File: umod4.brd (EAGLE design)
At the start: 104.9 x 69.8 mm, 94 parts, among them IC3 27C256-FEED-THRU, J2 10118194-0001LF, M1 RPi Pico W, M2 Generic single-sided NEO-8, Q1 C10487/SI2301CDS, Q2 SS8050, Q3 C10487/SI2301CDS, Q4 C10487/SI2301CDS, U1 74LVC541, U2 74LVC4245, U3 74LVC541, U4 RP2040, U5 W25Q128JVSIQ, U6 74LVC2G04, U8 3.3V/150mA, Y1 12MHz

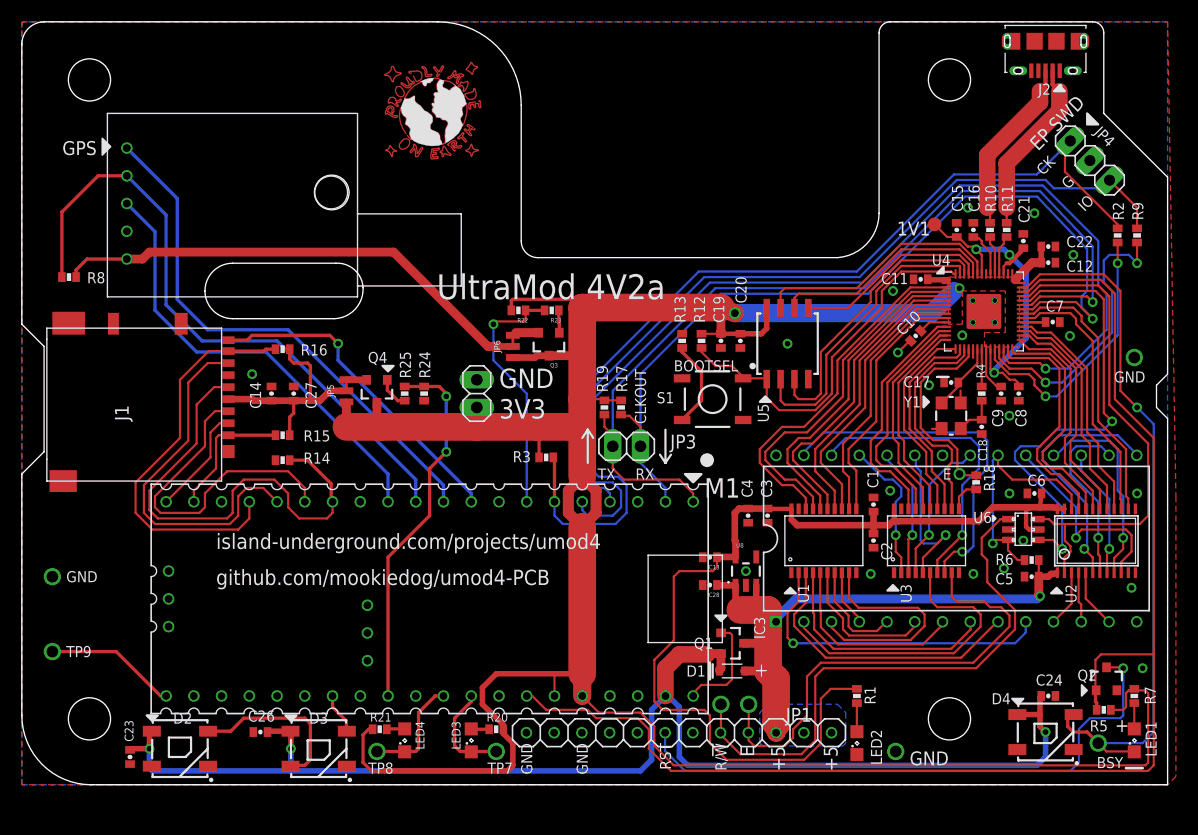
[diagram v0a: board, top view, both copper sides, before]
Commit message: 4v2a Release: add caps, DNP convention, production automation
Board changes:
- See Changelist-4V2.md for details

Tooling:
- Add preproduction.py: BOM generation (HTML + CSV), CPL generation via Eagle ULP batch mode, gerber freshness check, and ZIP packaging
- Add jlcpcb_smta_exporter_v7.ulp: modified to accept batch-mode arguments, bypassing interactive dialogs when invoked from script
- Update jlcpcb_2_layer_v72.cam: output path changed to build/cam/
- Update .gitignore: build/ directory rules with build/cam/.gitkeep anchor

Documentation:
- Add Production.md: describes end-to-end JLCPCB submission workflow
- Remove TestPlan.md
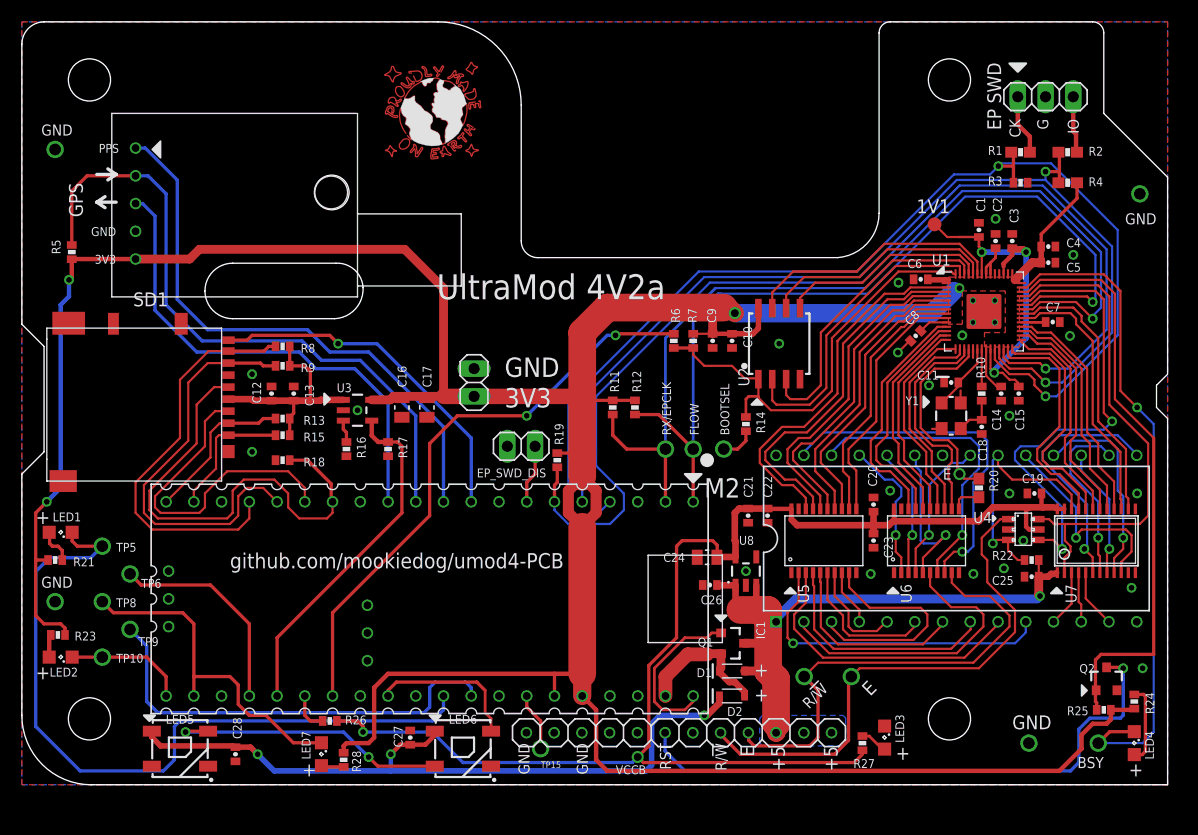
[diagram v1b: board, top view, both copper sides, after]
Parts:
- removed D3, D4: C2761795/WS2812B, SparkFun-LED:WS2812B
- removed J2: 10118194-0001LF, 10118194-0001LF:AMPHENOL_10118194-0001LF
- removed JP5, JP6: JUMPER-SMT_3_1-NC_TRACE_NO-SILK, SparkFun-Jumpers:SMT-JUMPER_3_1-NC_TRACE_NO-SILK
- removed Q3, Q4: C10487/SI2301CDS, robins-v7:SOT23
- removed S1: (no value), robins-v7:SW-TAC-5.2MM
- added C25: 100n/16V/X7R, SparkFun-03-01-2010:0402-CAP
- added LED5, LED6: WS2812, SparkFun-LED:WS2812B
- added LED7: NCD0805R1, led:SML0805
- added R26: 10K, SparkFun-03-01-2010:0402-RES
- added R27: 1K, SparkFun-03-01-2010:0402-RES
- added R28: 470R, SparkFun-03-01-2010:0402-RES
- added TP10, TP11, TP12, TP13, TP14, TP15, TP16: 1035, robins-v7:KEYSTONE-1035
- added U7: 74LVC4245, robins-v7:TSSOP-24
- C10, C3: value 100n/16V/X7R -> 2u2/6.3V/X5R
- C11: value 100n/16V/X7R -> 33p/6.3V/COG
- C13: value 1u/25V/X5R -> 4u7/10V/X5R
- C16, C24: value 100n/16V/X7R -> 10u/25V/X5R; device SparkFun-03-01-2010:0402-CAP -> robins-v7:SMD-0805
- C17: value 33p/6.3V/COG -> 10u/25V/X5R; device SparkFun-03-01-2010:0402-CAP -> robins-v7:SMD-0805
- C2, C28: value 1u/25V/X5R -> 100n/16V/X7R
- C20, C22: value 2u2/6.3V/X5R -> 100n/16V/X7R
- C21: value 2u2/6.3V/X5R -> 1u/25V/X5R
- C23: value 100n/16V/X7R -> 1u/25V/X5R
- C26: value 100n/16V/X7R -> 4u7/10V/X5R
- C27: value 4u7/10V/X5R -> 100n/16V/X7R
- C4: value 1u/25V/X5R -> 2u2/6.3V/X5R
- D2: value C2761795/WS2812B -> 1N5819WS; device SparkFun-LED:WS2812B -> SparkFun-DiscreteSemi:SOD-323
- JP1: value PINHD-1X12 -> (none); device robins:1X12 -> pinhead:1X03
- JP4: value (none) -> PINHD-1X12; device pinhead:1X03 -> robins:1X12
- LED3: value KT-0805G -> KT-0805Y
- M1: value RPi Pico W -> Generic single-sided NEO-8; device robins-v7:PICO-TH -> robins-v7:GPS-MODULE-DS
- M2: value Generic single-sided NEO-8 -> RPi Pico W; device robins-v7:GPS-MODULE-DS -> robins-v7:PICO-TH
- Q1: value C10487/SI2301CDS -> DNP/SI2301CDS
- R1: value 1K -> 100R; device SparkFun-03-01-2010:0402-RES -> SparkFun-03-01-2010:0603-RES
- R10: value 27R -> 1K
- R11, R18: value 27R -> 10K
- R13, R25: value 1K -> 10K
- R14, R6: value 10K -> 1K
- R2: device SparkFun-03-01-2010:0402-RES -> SparkFun-03-01-2010:0603-RES
- R20: value 470R -> 100R; device SparkFun-03-01-2010:0402-RES -> SparkFun-03-01-2010:0603-RES
- R23: value 1K -> 470R
- R24: value 10K -> 470R
- R4: value 1K -> 4K7; device SparkFun-03-01-2010:0402-RES -> SparkFun-03-01-2010:0603-RES
- R7: value 470R -> 10K
- R9: value 100R -> 10K
- SD1: value (none) -> DM3AT-SF-PEJM5
- TP1, TP2, TP3, TP4, TP5, TP6, TP7, TP8, TP9: value (none) -> 1035
- U1: value 74LVC541 -> RP2040; device robins-v7:TSSOP-20 -> robins-v7:RP2040-QFN56
- U2: value 74LVC4245 -> W25Q128JVSIQ; device robins-v7:TSSOP-24 -> SparkFun-IC-Memory:SOIC-8
- U3: value 74LVC541 -> SY6280AAC; device robins-v7:TSSOP-20 -> robins-v7:SOT23-5
- U4: value RP2040 -> 74LVC2G04; device robins-v7:RP2040-QFN56 -> robins-v7:SOT23-6
- U5: value W25Q128JVSIQ -> 74LVC541; device SparkFun-IC-Memory:SOIC-8 -> robins-v7:TSSOP-20
- U6: value 74LVC2G04 -> 74LVC541; device robins-v7:SOT23-6 -> robins-v7:TSSOP-20
- U8: value 3.3V/150mA -> TLV75733P
- moved R5 103.4 mm to (4.57, 48.8), turned to 270 degrees
- moved LED1 100.1 mm to (3.56, 23.1), turned to 180 degrees
- moved R9 79.1 mm to (23.9, 38.4), turned to 0 degrees
- moved LED2 73.3 mm to (3.56, 11.7), turned to 180 degrees
- moved C12 72.1 mm to (22.9, 35.8), turned to 90 degrees
- moved C23 70.9 mm to (78.0, 22.4)
- moved R24 70.9 mm to (101.9, 7.62)
- moved R25 70.3 mm to (99.1, 6.86), turned to 0 degrees
- moved JP1 67.2 mm to (93.7, 63.0)
- moved LED4 66.8 mm to (101.9, 3.81), turned to 270 degrees
- moved C14 66.8 mm to (89.7, 35.8), turned to 270 degrees
- moved JP4 64.5 mm to (60.2, 4.76), turned to 0 degrees
- moved R18 63.5 mm to (23.9, 29.7), turned to 180 degrees
- moved TP4 62.6 mm to (64.3, 30.7)
- moved TP5 60.9 mm to (7.37, 21.8)
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- renumbered IC3 to IC1, J1 to SD1
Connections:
- removed net 3V3_GPS_EN: M1.7, R22.1, R23.2
- removed net 3V3_SD_EN: M1.29, R24.2, R25.1
- removed net 3V3_SD_SW: JP5.3, Q4.S
- removed net 3V3_SW: JP6.3, Q3.S
- removed net N$15: R10.2, U4.47
- removed net N$16: R9.1, U4.25
- removed net N$17: J2.2, R11.1
- removed net N$18: J2.3, R10.1
- removed net N$23: Q4.G, R25.2
- removed net N$25: Q3.G, R23.1
- removed net SPARE0: LED3.C, M1.32, TP7.P$1
- removed net SPARE1: LED4.C, M1.31, TP8.P$1
- removed net SPARE2: M1.21, TP9.P$1
- removed net VCC_GPS: JP6.2, M2.5, R8.2
- new net DISK_BSY: LED1.C, M2.31, TP5.P$1
- new net EN_VDD_SD: M2.25, R17.1, U3.4
- new net EP_BOOTSEL: M2.27, R6.2
- new net EP_SWD_DIS: JP3.1, M2.7
- new net EXT_RP_SWCLK: JP1.1, R1.2
- new net EXT_RP_SWD: JP1.3, R2.2
- new net SPARE0_ADC: M2.32, TP9.P$1
- new net SPARE3: LED2.C, M2.21, TP10.P$1
- new net SPARE4: LED7.C, M2.22, TP8.P$1
- new net SPARE5: M2.24, TP6.P$1
- new net SPARE6_ADC: M2.34, TP15.P$1
- new net VCCB_PWR: M2.26, R26.2
- new net VLED: C27.1, C28.1, D2.C, LED5.1, LED6.1
- net !CARD: now also M2.9; no longer M1.9
- net !CE!_5V: now also R22.1, U4.3, U7.22; no longer R6.1, U2.22, U6.3
- net !RESET!_5V: now also JP4.6; no longer JP1.6
- net !RESET!_HC11_OUT: now also R25.1, U1.40; no longer M1.34, R5.1, U4.40
- net +3V3: now also C14.1, C17.1, C2.1, C4.1, C5.1, C6.1, C8.1, M1.5, M2.35, M2.36, R11.1, R12.1, R19.2, R23.1, R24.1, R25.2, R28.1, R4.1, R7.2, U1.1, U1.10, U1.22, U1.33, U1.42, U1.43, U1.44, U1.48, U1.49, U2.8, U3.5; no longer C11.1, C12.1, C19.1, C20.1, C22.1, JP5.1, JP6.1, M1.35, M1.36, Q3.D, Q4.D, R12.2, R17.1, R19.1, R20.1, R22.2, R3.2, R7.1, U4.1, U4.10, U4.22, U4.33, U4.42, U4.43, U4.44, U4.48, U4.49, U5.8
- net +5_ECU: now also C25.1, C26.1, JP4.10, JP4.12, R22.2, U7.1; no longer C28.1, C5.1, JP1.10, JP1.12, R6.2, U2.1
- net 1.0V: now also C1.1, C3.1, U1.23, U1.45, U1.50; no longer C21.1, C8.1, U4.23, U4.45, U4.50
- net A0_5V: now also U5.2; no longer U1.2
- net A10_5V: now also U6.4; no longer U3.4
- net A11_5V: now also U6.5; no longer U3.5
- net A12_5V: now also U6.6; no longer U3.6
- net A13_5V: now also U6.7; no longer U3.7
- net A14_5V: now also U6.8; no longer U3.8
- net A1_5V: now also U5.3; no longer U1.3
- net A2_5V: now also U5.4; no longer U1.4
- net A3_5V: now also U5.5; no longer U1.5
- net A4_5V: now also U5.6; no longer U1.6
- net A5_5V: now also U5.7; no longer U1.7
- net A6_5V: now also U5.8; no longer U1.8
- net A7_5V: now also U5.9; no longer U1.9
- net A8_5V: now also U6.2; no longer U3.2
- net A9_5V: now also U6.3; no longer U3.3
- net CE: now also U1.38, U4.4; no longer U4.38, U6.4
- net D0: now also U1.27, U7.21; no longer U2.21, U4.27
- net D0_5V: now also U7.3; no longer U2.3
- net D1: now also U1.28, U7.20; no longer U2.20, U4.28
- net D1_5V: now also U7.4; no longer U2.4
- net D2: now also U1.29, U7.19; no longer U2.19, U4.29
- net D2_5V: now also U7.5; no longer U2.5
- net D3: now also U1.30, U7.18; no longer U2.18, U4.30
- net D3_5V: now also U7.6; no longer U2.6
- net D4: now also U1.31, U7.17; no longer U2.17, U4.31
- net D4_5V: now also U7.7; no longer U2.7
- net D5: now also U1.32, U7.16; no longer U2.16, U4.32
- net D5_5V: now also U7.8; no longer U2.8
- net D6: now also U1.34, U7.15; no longer U2.15, U4.34
- net D6_5V: now also U7.9; no longer U2.9
- net D7: now also U1.35, U7.14; no longer U2.14, U4.35
- net D7_5V: now also U7.10; no longer U2.10
- net DAT1: now also M2.17, R8.1; no longer M1.17, R16.1
- net DAT2: now also M2.19; no longer M1.19
- net DBG_BSY: now also LED4.C, TP14.P$1, U1.41; no longer D4.4, LED1.C, TP1.P$1, U4.41
- net E: now also R20.1, U1.18; no longer R18.1, U4.18
- net EP_RUN: now also M2.6, R19.1, U1.26; no longer M1.6, R3.1, U4.26
- net E_5V: now also JP4.9, TP11.P$1, U6.9; no longer JP1.9, TP5.P$1, U3.9
- net GND: now also C11.1, C17.2, C25.2, JP1.2, JP3.2, JP4.1, JP4.3, LED3.C, LED5.3, LED6.3, M1.4, M2.13, M2.18, M2.23, M2.28, M2.3, M2.33, M2.38, M2.42, M2.45, M2.8, R16.2, R17.2, R18.2, R3.2, TP1.P$1, TP13.P$1, TP16.P$1, TP7.P$1, U1.57, U1.GND@1, U1.GND@2, U1.GND@3, U1.GND@4, U2.4, U3.2, U4.2, U5.1, U5.10, U5.19, U6.1, U6.10, U6.19, U7.11, U7.12, U7.13; no longer C11.2, C17.1, D2.3, D3.3, D4.3, J2.5, JP1.1, JP1.3, JP4.2, LED2.C, M1.13, M1.18, M1.23, M1.28, M1.3, M1.33, M1.38, M1.42, M1.45, M1.8, M2.4, R13.2, R14.2, R24.1, TP2.P$1, TP3.P$1, TP4.P$1, U1.1, U1.10, U2.11, U2.12, U2.13, U3.1, U3.10, U3.19, U4.19, U4.57, U4.GND@1, U4.GND@2, U4.GND@3, U4.GND@4, U5.4, U6.2
- net GPS_PPS: now also M1.1, M2.10; no longer M1.10, M2.1
- net IO0: now also U1.2, U5.18; no longer U1.18, U4.2
- net IO1: now also U1.3, U5.17; no longer U1.17, U4.3
- net IO10: now also U1.13, U6.16; no longer U3.16, U4.13
- net IO11: now also U1.14, U6.15; no longer U3.15, U4.14
- net IO12: now also U1.15, U6.14; no longer U3.14, U4.15
- net IO13: now also U1.16, U6.13; no longer U3.13, U4.16
- net IO14: now also U1.17, U6.12; no longer U3.12, U4.17
- net IO2: now also U1.4, U5.16; no longer U1.16, U4.4
- net IO3: now also U1.5, U5.15; no longer U1.15, U4.5
- net IO4: now also U1.6, U5.14; no longer U1.14, U4.6
- net IO5: now also U1.7, U5.13; no longer U1.13, U4.7
- net IO6: now also U1.8, U5.12; no longer U1.12, U4.8
- net IO7: now also U1.9, U5.11; no longer U1.11, U4.9
- net IO8: now also U1.11, U6.18; no longer U3.18, U4.11
- net IO9: now also U1.12, U6.17; no longer U3.17, U4.12
- net N$1: now also R10.2; no longer R4.2
- net N$10: now also U1.55, U2.2; no longer U4.55, U5.2
- net N$11: now also U1.54, U2.3; no longer U4.54, U5.3
- net N$12: now also U1.51, U2.7; no longer U4.51, U5.7
- net N$13: now also LED2.A, R23.2; no longer R11.2, U4.46
- net N$14: now also R16.1, U3.3; no longer R13.1, S1.1@1, S1.1@2
- net N$19: now also LED5.4, LED6.2; no longer D2.4, D3.2
- net N$2: now also C11.2, U1.20; no longer C17.2, U4.20
- net N$20: now also R20.2, U6.11; no longer R18.2, U3.11
- net N$21: now also LED1.A, R21.2; no longer LED3.A, R20.2
- net N$22: now also LED7.A, R28.2; no longer LED4.A, R21.2
- net N$3: now also LED3.A, R27.2; no longer LED2.A, R1.2
- net N$4: now also R14.1, TP4.P$1; no longer R2.1, U4.24
- net N$5: now also R10.1, U1.21; no longer R4.1, U4.21
- net N$6: now also LED4.A, R24.2; no longer LED1.A, R7.2
- net N$7: now also R14.2, R6.1, R7.1, U1.56, U2.1; no longer R12.1, S1.2@1, S1.2@2, U4.56, U5.1
- net N$8: now also U1.52, U2.6; no longer U4.52, U5.6
- net N$9: now also U1.53, U2.5; no longer U4.53, U5.5
- net PICOW_U0_RX: now also M2.2, R11.2, TP2.P$1, U1.36; no longer JP3.1, M1.2, R17.2, U4.36
- net PICOW_U0_TX: now also M2.1, R12.2, TP3.P$1, U1.37; no longer JP3.2, M1.1, R19.2, U4.37
- net PICOW_U1_RX: now also M1.3, M2.12; no longer M1.12, M2.3
- net PICOW_U1_TX: now also M1.2, M2.11, R5.1; no longer M1.11, M2.2, R8.1
- net R/!W!_5V: now also JP4.8, TP12.P$1, U4.1; no longer JP1.8, TP6.P$1, U6.1
- net RP_SWCLK: now also M2.4, R1.1, R3.1, U1.24; no longer JP4.1, M1.4, R2.2
- net RP_SWD: now also M2.5, R2.1, R4.2, U1.25; no longer JP4.3, M1.5, R9.2
- net SPI1_CS: now also M2.20, R13.1; no longer M1.20
- net SPI1_MISO: now also M2.16, R9.1; no longer M1.16
- net SPI1_MOSI: now also M2.15; no longer M1.15
- net SPI1_SCK: now also M2.14, R18.1; no longer M1.14, R14.1
- net VBUS: now also M2.40; no longer M1.40
- net VCCB: now also C19.1, C20.1, C21.1, C22.1, C23.1, C24.1, R26.1, R27.1, U4.5, U5.20, U6.20, U7.23, U7.24; no longer C1.1, C13.1, C2.1, C3.1, C4.1, C6.1, R1.1, U1.20, U2.23, U2.24, U3.20, U6.5
- net VDD_SD: now also C12.1, C13.1, R13.2, R8.2, R9.2, U3.1; no longer C14.1, C27.1, JP5.2, R16.2
- net VSYS: now also D2.A, M2.39; no longer C23.1, C24.1, C26.1, D2.1, D3.1, D4.1, M1.39
- net W/!R!: now also U1.39, U4.6, U7.2; no longer U2.2, U4.39, U6.6
- net WP_RUN: now also M2.30; no longer M1.30
- net WS2812_DI: now also LED6.4, M2.29; no longer D3.4, M1.27
- net XIRQ_5V: now also JP4.4; no longer JP1.4
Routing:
- net VSYS: track 123.2 -> 13.2 mm, vias 3 -> 0
- net !RESET!_HC11_OUT: track 125.9 -> 54.2 mm
- net DISK_BSY: track 0.00 -> 69.4 mm
- net VLED: track 0.00 -> 66.0 mm, vias 0 -> 3
- net +3V3: track 262.5 -> 317.8 mm, vias 2 -> 4
- net EP_BOOTSEL: track 0.00 -> 53.3 mm, vias 0 -> 2
- net VCC_GPS: track 44.9 -> 0.00 mm
- net SPARE0_ADC: track 0.00 -> 40.5 mm
- net 3V3_SD_EN: track 34.0 -> 0.00 mm, vias 2 -> 0
- net EN_VDD_SD: track 0.00 -> 32.1 mm
- net VCCB: track 91.2 -> 123.1 mm, vias 0 -> 2
- net SPARE4: track 0.00 -> 31.1 mm
- net RP_SWCLK: track 76.8 -> 106.3 mm, vias 0 -> 2
- net N$16: track 26.4 -> 0.00 mm, vias 2 -> 0
- net 3V3_GPS_EN: track 23.2 -> 0.00 mm, vias 1 -> 0
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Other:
- board text added: "EP_SWD_DIS"
- board text added: "FLOW"
- board text added: "PPS"
- board text added: "RX/EPCLK"
- board text added: "VCCB"
- board text removed: "CLKOUT"
- board text removed: "RX"
- board text removed: "TX"
- board text removed: "island-underground.com/projects/umod4"

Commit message: Replace 470R 0402 package with SMD-0603-NOM
- Affected parts: R21, R23, R24, R28
- LCSC_PART changes from C25117 to C23179
- Manually reworked wire angles on board to clear DRC failures
  from the new pad geometry
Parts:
- R21, R23, R24, R28: device SparkFun-03-01-2010:0402-RES -> robins-v7:SMD-0603-NOM
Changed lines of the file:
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@@
 <attribute name="LCSC_PART" value="C25744" x="92.456" y="20.574" size="1.778" layer="27" display="off"/>
 </element>
-<element name="R24" library="SparkFun-03-01-2010" package="0402-RES" value="470R" x="101.854" y="7.62" smashed="yes" rot="R90">
+<element name="R24" library="robins-v7" package="SMD-0603-NOM" value="470R" x="101.854" y="7.62" smashed="yes" rot="R90">
 <attribute name="NAME" x="103.6955" y="6.477" size="0.8128" layer="25" font="vector" ratio="14" rot="R90"/>
 <attribute name="VALUE" x="102.997" y="6.5405" size="0.4064" layer="27" rot="R90"/>
-<attribute name="LCSC_PART" value="C25117" x="101.854" y="7.62" size="1.778" layer="27" rot="R90" display="off"/>
+<attribute name="LCSC_PART" value="C23179" x="101.854" y="7.62" size="1.778" layer="27" rot="R90" display="off"/>
 </element>
 <element name="TP14" library="robins-v7" package="KEYSTONE-1035" value="1035" x="98.552" y="3.81" smashed="yes" rot="R180">
@@
 <attribute name="VALUE" x="18.415" y="3.8735" size="0.4064" layer="27" rot="R270"/>
 </element>
-<element name="R21" library="SparkFun-03-01-2010" package="0402-RES" value="470R" x="3.048" y="20.574" smashed="yes">
-<attribute name="LCSC_PART" value="C25117" x="-0.254" y="25.908" size="1.778" layer="27" display="off"/>
+<element name="R21" library="robins-v7" package="SMD-0603-NOM" value="470R" x="3.048" y="20.574" smashed="yes">
+<attribute name="LCSC_PART" value="C23179" x="-0.254" y="25.908" size="1.778" layer="27" display="off"/>
 <attribute name="NAME" x="4.699" y="20.0025" size="0.8128" layer="25" font="vector" ratio="14"/>
 <attribute name="VALUE" x="1.9685" y="19.431" size="0.4064" layer="27"/>
@@
 <attribute name="VALUE" x="5.056" y="25.114" size="1.27" layer="27" rot="R180"/>
 </element>
-<element name="R28" library="SparkFun-03-01-2010" package="0402-RES" value="470R" x="29.464" y="2.286" smashed="yes" rot="R270">
-<attribute name="LCSC_PART" value="C25117" x="34.798" y="5.588" size="1.778" layer="27" rot="R270" display="off"/>
+<element name="R28" library="robins-v7" package="SMD-0603-NOM" value="470R" x="29.464" y="2.286" smashed="yes" rot="R270">
+<attribute name="LCSC_PART" value="C23179" x="34.798" y="5.588" size="1.778" layer="27" rot="R270" display="off"/>
 <attribute name="NAME" x="31.0515" y="1.143" size="0.8128" layer="25" font="vector" ratio="14" rot="R90"/>
 <attribute name="VALUE" x="28.321" y="3.3655" size="0.4064" layer="27" rot="R270"/>
@@
 <attribute name="VALUE" x="8.636" y="16.764" size="0.8128" layer="27" font="vector" ratio="16"/>
 </element>
-<element name="R23" library="SparkFun-03-01-2010" package="0402-RES" value="470R" x="3.302" y="13.716" smashed="yes" rot="R180">
-<attribute name="LCSC_PART" value="C25117" x="7.366" y="8.382" size="1.778" layer="27" rot="R180" display="off"/>
+<element name="R23" library="robins-v7" package="SMD-0603-NOM" value="470R" x="3.302" y="13.716" smashed="yes" rot="R180">
+<attribute name="LCSC_PART" value="C23179" x="7.366" y="8.382" size="1.778" layer="27" rot="R180" display="off"/>
 <attribute name="NAME" x="4.826" y="13.208" size="0.8128" layer="25" font="vector" ratio="14"/>
 <attribute name="VALUE" x="4.3815" y="14.859" size="0.4064" layer="27" rot="R180"/>
@@
 <wire x1="99.71" y1="6.858" x2="99.71" y2="5.984" width="0.4064" layer="1"/>
 <wire x1="99.71" y1="6.858" x2="101.742" y2="6.858" width="0.4064" layer="1"/>
-<wire x1="101.742" y1="6.858" x2="101.854" y2="6.97" width="0.4064" layer="1"/>
-<wire x1="3.952" y1="13.716" x2="3.952" y2="14.336" width="0.3048" layer="1"/>
-<wire x1="3.952" y1="14.336" x2="3.556" y2="14.732" width="0.3048" layer="1"/>
 <wire x1="3.556" y1="14.732" x2="2.032" y2="14.732" width="0.3048" layer="1"/>
 <wire x1="2.032" y1="14.732" x2="1.27" y2="15.494" width="0.3048" layer="1"/>
@@
 <wire x1="2.286" y1="25.908" x2="3.556" y2="27.178" width="0.4064" layer="16"/>
 <wire x1="1.27" y1="24.892" x2="2.286" y2="25.908" width="0.3048" layer="1"/>
-<wire x1="2.398" y1="20.574" x2="1.27" y2="20.574" width="0.3048" layer="1"/>
+<wire x1="2.223" y1="20.574" x2="1.27" y2="20.574" width="0.3048" layer="1"/>
 <wire x1="33.716" y1="35.24" x2="34.036" y2="35.56" width="0.8128" layer="1"/>
 <wire x1="34.036" y1="35.56" x2="34.29" y2="35.56" width="0.8128" layer="1"/>
@@
 <wire x1="34.29" y1="35.444" x2="34.29" y2="35.56" width="0.4064" layer="1"/>
 <wire x1="37.084" y1="35.444" x2="37.592" y2="35.444" width="0.4064" layer="1"/>
-<wire x1="29.464" y1="2.936" x2="29.464" y2="3.556" width="0.4064" layer="1"/>
+<wire x1="29.464" y1="3.111" x2="29.464" y2="3.556" width="0.4064" layer="1"/>
 <wire x1="29.464" y1="3.556" x2="29.718" y2="3.81" width="0.4064" layer="1"/>
 <wire x1="29.718" y1="3.81" x2="31.75" y2="3.81" width="0.4064" layer="1"/>
@@
 <wire x1="52.578" y1="2.286" x2="52.578" y2="6.858" width="0.4064" layer="1"/>
 <wire x1="52.578" y1="6.858" x2="51.308" y2="8.128" width="0.4064" layer="1"/>
+<wire x1="4.127" y1="13.716" x2="4.127" y2="14.161" width="0.3048" layer="1"/>
+<wire x1="4.127" y1="14.161" x2="3.556" y2="14.732" width="0.3048" layer="1"/>
+<wire x1="90.932" y1="46.228" x2="91.5247" y2="45.9324" width="0" layer="19" extent="1-1"/>
+<wire x1="90.6872" y1="46.7699" x2="90.932" y2="46.228" width="0" layer="19" extent="1-1"/>
+<wire x1="90.2872" y1="46.7699" x2="90.6872" y2="46.7699" width="0" layer="19" extent="1-1"/>
+<wire x1="88.6872" y1="46.7699" x2="90.2872" y2="46.7699" width="0" layer="19" extent="1-1"/>
+<wire x1="85.852" y1="45.72" x2="88.2872" y2="46.7699" width="0" layer="19" extent="1-16"/>
+<wire x1="83.0844" y1="42.3324" x2="83.312" y2="43.18" width="0" layer="19" extent="1-16"/>
+<wire x1="84.6497" y1="45.9324" x2="85.344" y2="45.212" width="0" layer="19" extent="1-16"/>
+<wire x1="91.5247" y1="42.3324" x2="91.5247" y2="45.9324" width="0" layer="19" extent="1-1"/>
+<wire x1="88.2872" y1="39.8949" x2="91.5247" y2="42.3324" width="0" layer="19" extent="1-1"/>
+<wire x1="101.854" y1="6.795" x2="101.805" y2="6.795" width="0.3048" layer="1"/>
+<wire x1="101.805" y1="6.795" x2="101.742" y2="6.858" width="0.3048" layer="1"/>
 </signal>
 <signal name="R/!W!_5V">
@@
 <contactref element="R24" pad="2"/>
 <contactref element="LED4" pad="A"/>
-<wire x1="101.854" y1="8.27" x2="102.728" y2="8.27" width="0.3048" layer="1"/>
-<wire x1="102.728" y1="8.27" x2="102.87" y2="8.128" width="0.3048" layer="1"/>
 <wire x1="101.854" y1="2.76" x2="102.582" y2="2.76" width="0.3048" layer="1"/>
 <wire x1="102.582" y1="2.76" x2="102.87" y2="3.048" width="0.3048" layer="1"/>
 <wire x1="102.87" y1="3.048" x2="102.87" y2="8.128" width="0.3048" layer="1"/>
+<wire x1="101.854" y1="8.445" x2="102.553" y2="8.445" width="0.3048" layer="1"/>
+<wire x1="102.553" y1="8.445" x2="102.87" y2="8.128" width="0.3048" layer="1"/>
 </signal>
 <signal name="N$7">
@@
 <contactref element="R21" pad="2"/>
 <contactref element="LED1" pad="A"/>
-<wire x1="3.698" y1="20.574" x2="3.698" y2="21.448" width="0.3048" layer="1"/>
-<wire x1="3.698" y1="21.448" x2="3.302" y2="21.844" width="0.3048" layer="1"/>
 <wire x1="3.302" y1="21.844" x2="2.794" y2="21.844" width="0.3048" layer="1"/>
 <wire x1="2.794" y1="21.844" x2="2.54" y2="22.098" width="0.3048" layer="1"/>
 <wire x1="2.54" y1="22.098" x2="2.54" y2="23.08" width="0.3048" layer="1"/>
 <wire x1="2.54" y1="23.08" x2="2.506" y2="23.114" width="0.3048" layer="1"/>
+<wire x1="3.873" y1="20.574" x2="3.873" y2="21.273" width="0.3048" layer="1"/>
+<wire x1="3.873" y1="21.273" x2="3.302" y2="21.844" width="0.3048" layer="1"/>
 </signal>
 <signal name="N$22">
 <contactref element="R28" pad="2"/>
 <contactref element="LED7" pad="A"/>
-<wire x1="29.464" y1="1.636" x2="27.54" y2="1.636" width="0.3048" layer="1"/>
-<wire x1="27.54" y1="1.636" x2="27.432" y2="1.744" width="0.3048" layer="1"/>
+<wire x1="29.464" y1="1.461" x2="28.511" y2="1.461" width="0.3048" layer="1"/>
+<wire x1="27.432" y1="1.744" x2="28.228" y2="1.744" width="0.3048" layer="1"/>
+<wire x1="28.228" y1="1.744" x2="28.511" y2="1.461" width="0.3048" layer="1"/>
 </signal>
 <signal name="VDD_SD">
@@
 <contactref element="LED2" pad="A"/>
 <wire x1="2.506" y1="11.684" x2="2.506" y2="13.57" width="0.4064" layer="1"/>
-<wire x1="2.506" y1="13.57" x2="2.652" y2="13.716" width="0.4064" layer="1"/>
+<wire x1="2.477" y1="13.716" x2="2.477" y2="13.599" width="0.3048" layer="1"/>
+<wire x1="2.477" y1="13.599" x2="2.506" y2="13.57" width="0.3048" layer="1"/>
 </signal>
 <signal name="EXT_RP_SWCLK">
